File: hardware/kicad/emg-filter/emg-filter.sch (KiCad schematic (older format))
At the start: 0 parts

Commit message: minor fixes
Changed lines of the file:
@@
 $EndDescr
 $Sheet
-S 1500 1500 1000 1000
+S 1250 1500 1000 1000
 U 61C38667
 F0 "power" 50
@@
 $EndSheet
 $Sheet
-S 3000 1500 1000 1000
+S 2750 1500 1000 1000
 U 61C386B1
 F0 "instrumentation" 50
@@
 $EndSheet
 $Sheet
-S 4500 1500 1000 1000
+S 4250 1500 1000 1000
 U 61C386E2
 F0 "bandpass" 50
@@
 $EndSheet
 $Sheet
-S 6000 1500 1000 1000
+S 5750 1500 1000 1000
 U 61C38708
 F0 "notch" 50
@@
 $EndSheet
 $Sheet
-S 7500 1500 1000 1000
+S 7250 1500 1000 1000
 U 61C38746
 F0 "rectifier" 50
@@
 $EndSheet
 $Sheet
-S 9000 1500 1000 1000
+S 8750 1500 1000 1000
 U 61C38776
 F0 "amplifier" 50
@@
 $EndSheet
 $Sheet
-S 1500 3000 1000 1000
+S 1250 3000 1000 1000
 U 61C38939
 F0 "adc" 50
@@
 $EndSheet
 $Sheet
-S 3000 3000 1000 1000
+S 2750 3000 1000 1000
 U 61C389A8
-F0 "connectors" 50
-F1 "connectors.sch" 50
+F0 "emg-connectors" 50
+F1 "emg-connectors.sch" 50
 $EndSheet
 Text Notes 550  850  0    197  ~ 39

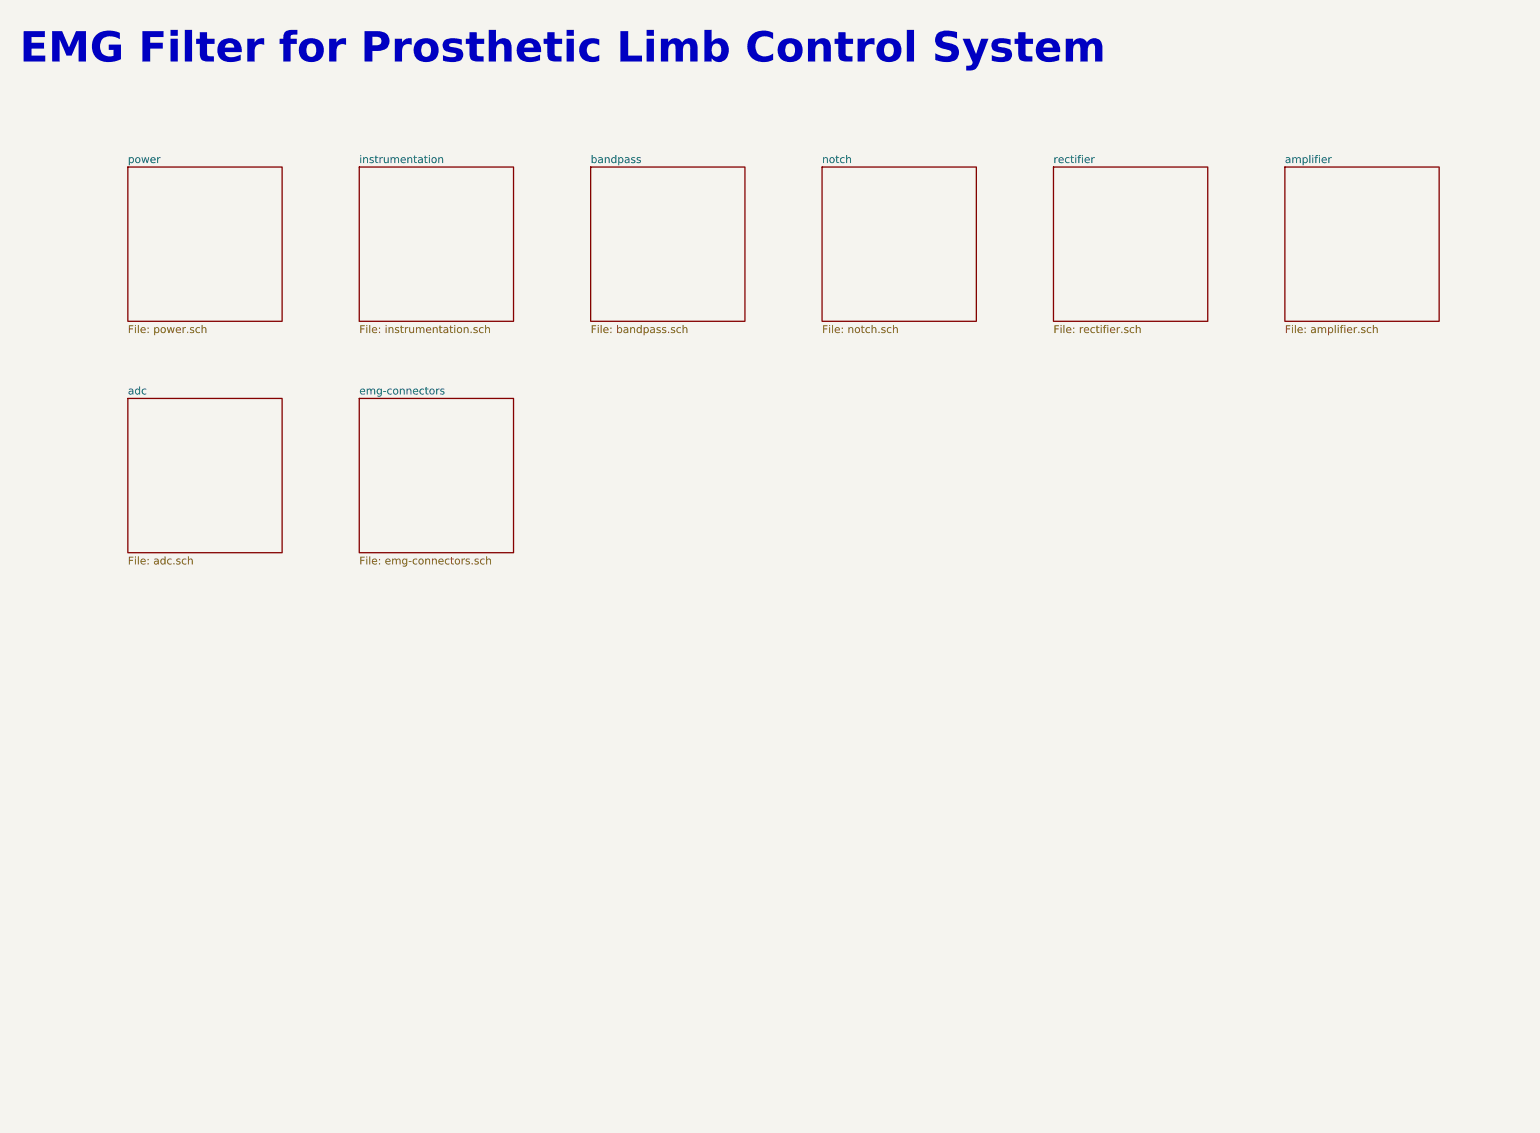
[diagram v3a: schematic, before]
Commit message: Block implementation
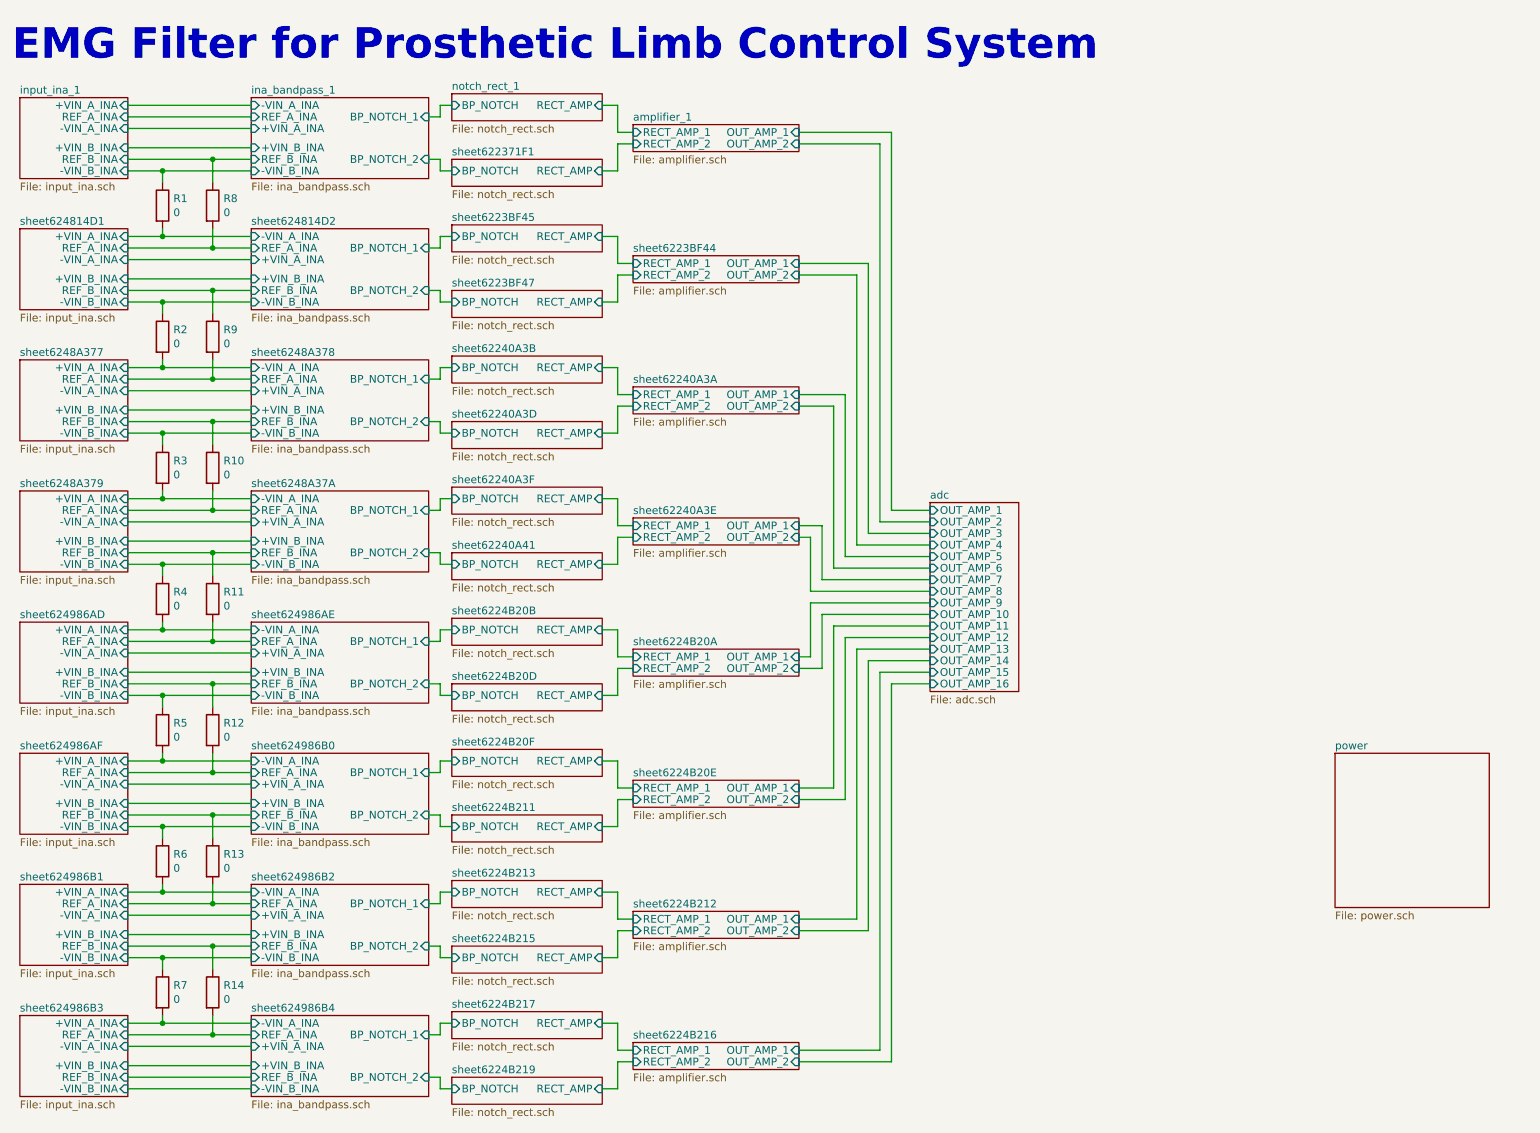
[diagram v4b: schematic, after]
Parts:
- added R1, R10, R11, R12, R13, R14, R2, R3, R4, R5, R6, R7, R8, R9: 0, Resistor_SMD:R_0805_2012Metric, symbol Device:R
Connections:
- new net ina_bandpass_1/-VIN_B_INA: R1.1
- new net ina_bandpass_1/REF_B_INA: R8.1
- new net sheet624814D1/+VIN_A_INA: R1.2
- new net sheet624814D1/-VIN_B_INA: R2.1
- new net sheet624814D1/REF_A_INA: R8.2
- new net sheet624814D1/REF_B_INA: R9.1
- new net sheet6248A377/+VIN_A_INA: R2.2
- new net sheet6248A377/-VIN_B_INA: R3.1
- new net sheet6248A377/REF_A_INA: R9.2
- new net sheet6248A377/REF_B_INA: R10.1
- new net sheet6248A379/+VIN_A_INA: R3.2
- new net sheet6248A379/-VIN_B_INA: R4.1
- new net sheet6248A379/REF_A_INA: R10.2
- new net sheet6248A379/REF_B_INA: R11.1
- new net sheet624986AD/+VIN_A_INA: R4.2
- new net sheet624986AD/-VIN_B_INA: R5.1
- new net sheet624986AD/REF_A_INA: R11.2
- new net sheet624986AD/REF_B_INA: R12.1
- new net sheet624986AF/+VIN_A_INA: R5.2
- new net sheet624986AF/-VIN_B_INA: R6.1
- new net sheet624986AF/REF_A_INA: R12.2
- new net sheet624986AF/REF_B_INA: R13.1
- new net sheet624986B1/+VIN_A_INA: R6.2
- new net sheet624986B1/-VIN_B_INA: R7.1
- new net sheet624986B1/REF_A_INA: R13.2
- new net sheet624986B1/REF_B_INA: R14.1
- new net sheet624986B3/+VIN_A_INA: R7.2
- new net sheet624986B3/REF_A_INA: R14.2

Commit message: compact design
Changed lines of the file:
@@
 $EndDescr
 $Sheet
-S 9075 5300 1000 1000
+S 9325 5575 1000 1000
 U 61C38667
 F0 "power" 50

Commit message: update
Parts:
- removed R10, R11, R12, R13, R14, R3, R4, R5, R6, R7: 0, Resistor_SMD:R_0805_2012Metric, symbol Device:R
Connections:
- wire segments 248 -> 42
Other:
- moved on the sheet: R1, R2, R8, R9

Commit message: update
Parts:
- added J? (x3): Conn_01x02, emg-filter:EMG_CONN_01x02, symbol Connector_Generic:Conn_01x02
- added J? (x2): Conn_01x05, symbol Connector_Generic:Conn_01x05
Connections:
- wire segments 42 -> 49
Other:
- moved on the sheet: R1, R2, R8, R9
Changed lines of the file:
@@
 Text Notes 500  825  0    197  ~ 39
 EMG Filter for Prosthetic Limb Control System
-Wire Wire Line
-	7150 3075 7600 3075
-Wire Wire Line
-	7525 3150 7150 3150
 $Sheet
 S 4900 3250 975  175
@@
 $EndSheet
 Wire Wire Line
-	2800 2400 3350 2400
-Wire Wire Line
-	2800 2325 3600 2325
-$Sheet
-S 2100 2850 700  525
+	4650 1375 5200 1375
+Wire Wire Line
+	4650 1300 5450 1300
+$Sheet
+S 1950 2850 850  525
 U 624814DA
 F0 "sheet624814D1" 50
@@
 	4825 3325 4900 3325
 Wire Wire Line
-	2800 3325 3025 3325
-Wire Wire Line
-	2800 3250 3350 3250
-Wire Wire Line
 	2800 3175 3600 3175
 Wire Wire Line
 	2800 3050 3600 3050
 Wire Wire Line
-	2800 2975 3350 2975
-Wire Wire Line
-	2800 2900 3025 2900
-Wire Wire Line
-	2800 3900 3600 3900
-Wire Wire Line
-	2800 3825 3350 3825
-Wire Wire Line
-	2800 3750 3025 3750
+	2800 2975 3250 2975
 $Comp
 L Device:R R?
 U 1 1 624AA066
-P 3025 2700
+P 4875 1675
 AR Path="/61C386B1/624AA066" Ref="R?"  Part="1"
 AR Path="/61C389A8/624AA066" Ref="R?"  Part="1"
@@
 AR Path="/62498716/624AA066" Ref="R?"  Part="1"
 AR Path="/624AA066" Ref="R1"  Part="1"
-F 0 "R1" H 3095 2746 50  0000 L CNN
-F 1 "0" H 3095 2655 50  0000 L CNN
-F 2 "Resistor_SMD:R_0805_2012Metric" V 2955 2700 50  0001 C CNN
-F 3 "~" H 3025 2700 50  0001 C CNN
-	1    3025 2700
+F 0 "R1" H 4945 1721 50  0000 L CNN
+F 1 "0" H 4945 1630 50  0000 L CNN
+F 2 "Resistor_SMD:R_0805_2012Metric" V 4805 1675 50  0001 C CNN
+F 3 "~" H 4875 1675 50  0001 C CNN
+	1    4875 1675
 	1    0    0    -1
 $EndComp
@@
 L Device:R R?
 U 1 1 624BBA9E
-P 3350 2700
+P 5200 1675
 AR Path="/61C386B1/624BBA9E" Ref="R?"  Part="1"
 AR Path="/61C389A8/624BBA9E" Ref="R?"  Part="1"
@@
 AR Path="/62498716/624BBA9E" Ref="R?"  Part="1"
 AR Path="/624BBA9E" Ref="R8"  Part="1"
-F 0 "R8" H 3420 2746 50  0000 L CNN
-F 1 "0" H 3420 2655 50  0000 L CNN
-F 2 "Resistor_SMD:R_0805_2012Metric" V 3280 2700 50  0001 C CNN
-F 3 "~" H 3350 2700 50  0001 C CNN
-	1    3350 2700
+F 0 "R8" H 5270 1721 50  0000 L CNN
+F 1 "0" H 5270 1630 50  0000 L CNN
+F 2 "Resistor_SMD:R_0805_2012Metric" V 5130 1675 50  0001 C CNN
+F 3 "~" H 5200 1675 50  0001 C CNN
+	1    5200 1675
 	1    0    0    -1
 $EndComp
 Wire Wire Line
-	2800 2475 3025 2475
-Wire Wire Line
-	3025 2475 3025 2550
-Connection ~ 3025 2475
-Wire Wire Line
-	3025 2475 3600 2475
-Wire Wire Line
-	3350 2400 3350 2550
-Connection ~ 3350 2400
-Wire Wire Line
-	3350 2400 3600 2400
-Wire Wire Line
-	3025 2850 3025 2900
-Connection ~ 3025 2900
-Wire Wire Line
-	3025 2900 3600 2900
-Wire Wire Line
-	3350 2850 3350 2975
-Connection ~ 3350 2975
-Wire Wire Line
-	3350 2975 3600 2975
+	4650 1450 4875 1450
+Wire Wire Line
+	4875 1450 4875 1525
+Connection ~ 4875 1450
+Wire Wire Line
+	4875 1450 5450 1450
+Wire Wire Line
+	5200 1375 5200 1525
+Connection ~ 5200 1375
+Wire Wire Line
+	5200 1375 5450 1375
+$Comp
+L Connector_Generic:Conn_01x02 J?
+U 1 1 61F541EB
+P 3250 2550
+AR Path="/61C386B1/61F541EB" Ref="J?"  Part="1"
+AR Path="/61C389A8/61F541EB" Ref="J?"  Part="1"
+AR Path="/622FC90E/61F541EB" Ref="J?"  Part="1"
+AR Path="/623EBE47/61F541EB" Ref="J?"  Part="1"
+AR Path="/624814DA/61F541EB" Ref="J?"  Part="1"
+AR Path="/6248A382/61F541EB" Ref="J?"  Part="1"
+AR Path="/6248A3A0/61F541EB" Ref="J?"  Part="1"
+AR Path="/624986BC/61F541EB" Ref="J?"  Part="1"
+AR Path="/624986DA/61F541EB" Ref="J?"  Part="1"
+AR Path="/624986F8/61F541EB" Ref="J?"  Part="1"
+AR Path="/62498716/61F541EB" Ref="J?"  Part="1"
+AR Path="/61F541EB" Ref="J?"  Part="1"
+F 0 "J?" H 3775 2550 50  0000 R CNN
+F 1 "Conn_01x02" H 3775 2450 50  0000 R CNN
+F 2 "emg-filter:EMG_CONN_01x02" H 3250 2550 50  0001 C CNN
+F 3 "~" H 3250 2550 50  0001 C CNN
+	1    3250 2550
+	0    1    -1   0
+$EndComp
+Wire Wire Line
+	3250 2750 3250 2975
+Connection ~ 3250 2975
+Wire Wire Line
+	3150 2750 3150 2900
+Connection ~ 3150 2900
+Wire Wire Line
+	3150 2900 3600 2900
+Wire Wire Line
+	2800 2900 3150 2900
+Wire Wire Line
+	3250 2975 3600 2975
+Wire Wire Line
+	2800 3250 3250 3250
+$Comp
+L Connector_Generic:Conn_01x02 J?
+U 1 1 61F5D7D3
+P 3250 3675
+AR Path="/61C386B1/61F5D7D3" Ref="J?"  Part="1"
+AR Path="/61C389A8/61F5D7D3" Ref="J?"  Part="1"
+AR Path="/622FC90E/61F5D7D3" Ref="J?"  Part="1"
+AR Path="/623EBE47/61F5D7D3" Ref="J?"  Part="1"
+AR Path="/624814DA/61F5D7D3" Ref="J?"  Part="1"
+AR Path="/6248A382/61F5D7D3" Ref="J?"  Part="1"
+AR Path="/6248A3A0/61F5D7D3" Ref="J?"  Part="1"
+AR Path="/624986BC/61F5D7D3" Ref="J?"  Part="1"
+AR Path="/624986DA/61F5D7D3" Ref="J?"  Part="1"
+AR Path="/624986F8/61F5D7D3" Ref="J?"  Part="1"
+AR Path="/62498716/61F5D7D3" Ref="J?"  Part="1"
+AR Path="/61F5D7D3" Ref="J?"  Part="1"
+F 0 "J?" H 3775 3675 50  0000 R CNN
+F 1 "Conn_01x02" H 3775 3575 50  0000 R CNN
+F 2 "emg-filter:EMG_CONN_01x02" H 3250 3675 50  0001 C CNN
+F 3 "~" H 3250 3675 50  0001 C CNN
+	1    3250 3675
+	0    1    1    0
+$EndComp
+Wire Wire Line
+	3250 3475 3250 3250
+Connection ~ 3250 3250
+Wire Wire Line
+	3150 3325 3150 3475
+Connection ~ 3150 3325
+Wire Wire Line
+	3150 3325 3600 3325
+Wire Wire Line
+	2800 3325 3150 3325
+Wire Wire Line
+	3250 3250 3600 3250
+$Comp
+L Connector_Generic:Conn_01x05 J?
+U 1 1 61F69EB5
+P 7725 3675
+F 0 "J?" V 7597 3955 50  0000 L CNN
+F 1 "Conn_01x05" V 7688 3955 50  0000 L CNN
+F 2 "" H 7725 3675 50  0001 C CNN
+F 3 "~" H 7725 3675 50  0001 C CNN
+	1    7725 3675
+	0    1    1    0
+$EndComp
+$Comp
+L Connector_Generic:Conn_01x05 J?
+U 1 1 61F6D9FD
+P 7725 2550
+F 0 "J?" V 7689 2830 50  0000 L CNN
+F 1 "Conn_01x05" V 7598 2830 50  0000 L CNN
+F 2 "" H 7725 2550 50  0001 C CNN
+F 3 "~" H 7725 2550 50  0001 C CNN
+	1    7725 2550
+	0    1    -1   0
+$EndComp
+Wire Wire Line
+	7725 2750 7725 3475
+Wire Wire Line
+	7525 2750 7525 3075
+Wire Wire Line
+	7625 3150 7150 3150
+Connection ~ 7625 3150
+Wire Wire Line
+	7625 3150 7625 3475
+Wire Wire Line
+	7625 2750 7625 3150
+Wire Wire Line
+	7525 3075 7150 3075
+Connection ~ 7525 3075
+Wire Wire Line
+	7525 3075 7525 3475
+Wire Wire Line
+	7825 2750 7825 3475
+Wire Wire Line
+	7925 3475 7925 2750
+Wire Wire Line
+	3000 4750 3575 4750
+Wire Wire Line
+	3000 4700 3000 4750
+Wire Wire Line
+	3325 4825 3575 4825
+Wire Wire Line
+	3325 4700 3325 4825
+$Comp
+L Device:R R?
+U 1 1 6274723C
+P 3325 4550
+AR Path="/61C386B1/6274723C" Ref="R?"  Part="1"
+AR Path="/61C389A8/6274723C" Ref="R?"  Part="1"
+AR Path="/622FC90E/6274723C" Ref="R?"  Part="1"
+AR Path="/623EBE47/6274723C" Ref="R?"  Part="1"
+AR Path="/624814DA/6274723C" Ref="R?"  Part="1"
+AR Path="/6248A382/6274723C" Ref="R?"  Part="1"
+AR Path="/6248A3A0/6274723C" Ref="R?"  Part="1"
+AR Path="/624986BC/6274723C" Ref="R?"  Part="1"
+AR Path="/624986DA/6274723C" Ref="R?"  Part="1"
+AR Path="/624986F8/6274723C" Ref="R?"  Part="1"
+AR Path="/62498716/6274723C" Ref="R?"  Part="1"
+AR Path="/6274723C" Ref="R9"  Part="1"
+F 0 "R9" H 3395 4596 50  0000 L CNN
+F 1 "0" H 3395 4505 50  0000 L CNN
+F 2 "Resistor_SMD:R_0805_2012Metric" V 3255 4550 50  0001 C CNN
+F 3 "~" H 3325 4550 50  0001 C CNN
+	1    3325 4550
+	1    0    0    -1
+$EndComp
 $Comp
 L Device:R R?
 U 1 1 62747236
-P 3025 3550
+P 3000 4550
 AR Path="/61C386B1/62747236" Ref="R?"  Part="1"
 AR Path="/61C389A8/62747236" Ref="R?"  Part="1"
@@
 AR Path="/62498716/62747236" Ref="R?"  Part="1"
 AR Path="/62747236" Ref="R2"  Part="1"
-F 0 "R2" H 3095 3596 50  0000 L CNN
-F 1 "0" H 3095 3505 50  0000 L CNN
-F 2 "Resistor_SMD:R_0805_2012Metric" V 2955 3550 50  0001 C CNN
-F 3 "~" H 3025 3550 50  0001 C CNN
-	1    3025 3550
+F 0 "R2" H 3070 4596 50  0000 L CNN
+F 1 "0" H 3070 4505 50  0000 L CNN
+F 2 "Resistor_SMD:R_0805_2012Metric" V 2930 4550 50  0001 C CNN
+F 3 "~" H 3000 4550 50  0001 C CNN
+	1    3000 4550
 	1    0    0    -1
 $EndComp
-$Comp
-L Device:R R?
-U 1 1 6274723C
-P 3350 3550
-AR Path="/61C386B1/6274723C" Ref="R?"  Part="1"
-AR Path="/61C389A8/6274723C" Ref="R?"  Part="1"
-AR Path="/622FC90E/6274723C" Ref="R?"  Part="1"
-AR Path="/623EBE47/6274723C" Ref="R?"  Part="1"
-AR Path="/624814DA/6274723C" Ref="R?"  Part="1"
-AR Path="/6248A382/6274723C" Ref="R?"  Part="1"
-AR Path="/6248A3A0/6274723C" Ref="R?"  Part="1"
-AR Path="/624986BC/6274723C" Ref="R?"  Part="1"
-AR Path="/624986DA/6274723C" Ref="R?"  Part="1"
-AR Path="/624986F8/6274723C" Ref="R?"  Part="1"
-AR Path="/62498716/6274723C" Ref="R?"  Part="1"
-AR Path="/6274723C" Ref="R9"  Part="1"
-F 0 "R9" H 3420 3596 50  0000 L CNN
-F 1 "0" H 3420 3505 50  0000 L CNN
-F 2 "Resistor_SMD:R_0805_2012Metric" V 3280 3550 50  0001 C CNN
-F 3 "~" H 3350 3550 50  0001 C CNN
-	1    3350 3550
-	1    0    0    -1
-$EndComp
-Wire Wire Line
-	3025 3400 3025 3325
-Connection ~ 3025 3325
-Wire Wire Line
-	3025 3325 3600 3325
-Wire Wire Line
-	3350 3400 3350 3250
-Connection ~ 3350 3250
-Wire Wire Line
-	3350 3250 3600 3250
-Wire Wire Line
-	3350 3700 3350 3825
-Connection ~ 3350 3825
-Wire Wire Line
-	3350 3825 3600 3825
-Wire Wire Line
-	3025 3700 3025 3750
-Connection ~ 3025 3750
-Wire Wire Line
-	3025 3750 3600 3750
+Connection ~ 3000 4750
+Wire Wire Line
+	2775 4750 3000 4750
+Connection ~ 3325 4825
+Wire Wire Line
+	2775 4825 3325 4825
+Wire Wire Line
+	2775 4900 3575 4900
+$Comp
+L Connector_Generic:Conn_01x02 J?
+U 1 1 61F7C54C
+P 3150 1600
+AR Path="/61C386B1/61F7C54C" Ref="J?"  Part="1"
+AR Path="/61C389A8/61F7C54C" Ref="J?"  Part="1"
+AR Path="/622FC90E/61F7C54C" Ref="J?"  Part="1"
+AR Path="/623EBE47/61F7C54C" Ref="J?"  Part="1"
+AR Path="/624814DA/61F7C54C" Ref="J?"  Part="1"
+AR Path="/6248A382/61F7C54C" Ref="J?"  Part="1"
+AR Path="/6248A3A0/61F7C54C" Ref="J?"  Part="1"
+AR Path="/624986BC/61F7C54C" Ref="J?"  Part="1"
+AR Path="/624986DA/61F7C54C" Ref="J?"  Part="1"
+AR Path="/624986F8/61F7C54C" Ref="J?"  Part="1"
+AR Path="/62498716/61F7C54C" Ref="J?"  Part="1"
+AR Path="/61F7C54C" Ref="J?"  Part="1"
+F 0 "J?" H 3675 1600 50  0000 R CNN
+F 1 "Conn_01x02" H 3675 1500 50  0000 R CNN
+F 2 "emg-filter:EMG_CONN_01x02" H 3150 1600 50  0001 C CNN
+F 3 "~" H 3150 1600 50  0001 C CNN
+	1    3150 1600
+	0    -1   1    0
+$EndComp
 $EndSCHEMATC
